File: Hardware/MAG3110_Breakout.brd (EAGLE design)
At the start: 15.2 x 15.2 mm, 18 parts, among them U1 MAG3110

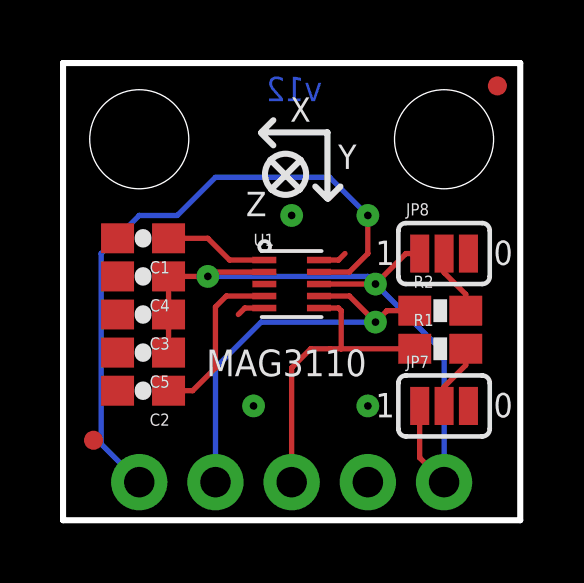
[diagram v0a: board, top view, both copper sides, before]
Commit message: Fixed pullup jumper and C3 position
Removed both three pad jumpers. Replaced with one jumper to pullup I2C
lines. Moved C3 closer to pin 8. Corrected 4 way VCC net in schematic.
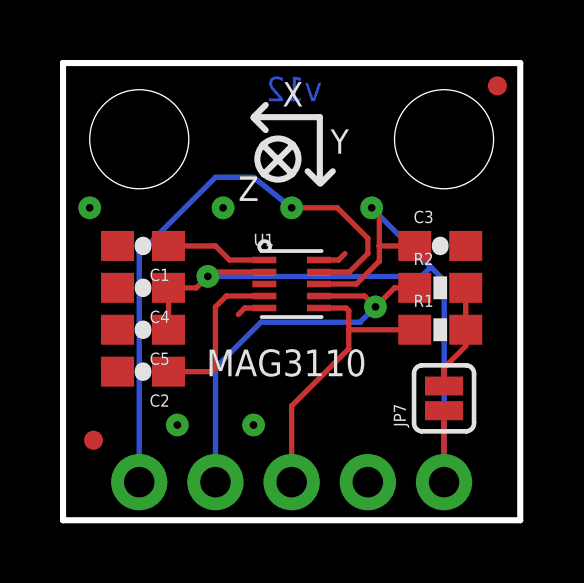
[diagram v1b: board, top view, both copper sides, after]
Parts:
- removed JP8: JUMPER-31-2, SparkFun-Passives:SJ_3_PASTE1&2
- JP7: value JUMPER-31-2 -> (none); device SparkFun-Passives:SJ_3_PASTE1&2 -> SparkFun-Passives:SJ_2S
- moved C3 10.2 mm to (12.6, 9.14), turned to 0 degrees
- moved C5 0.76 mm to (2.67, 6.35)
- moved R2 0.76 mm to (12.6, 7.75)
- moved C2 0.64 mm to (2.67, 4.95)
- moved JP4 0.63 mm to (8.43, 10.7)
- moved R1 0.63 mm to (12.6, 6.35)
- moved C4 0.38 mm to (2.67, 7.75)
- moved JP7 0.25 mm to (12.7, 4.06), turned to 90 degrees
- moved C1 0.25 mm to (2.67, 9.14)
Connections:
- removed net N$4: JP7.2, R1.2
- net GND: no longer JP7.3, JP8.3
- net N$3: now also JP7.2, R1.2; no longer JP8.2
- net VCC: no longer JP8.1
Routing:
- net VCC: track 25.7 -> 30.3 mm
- net INT: track 21.8 -> 19.5 mm
- net N$4: track 2.20 -> 0.00 mm
- net N$3: track 2.20 -> 3.57 mm
- net GND: vias 3 -> 4
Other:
- board text removed: "0"
- board text removed: "1"

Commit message: Updated main IC to 1:1
Updated footprint on main IC to 1:1 for better reflow and AOI.
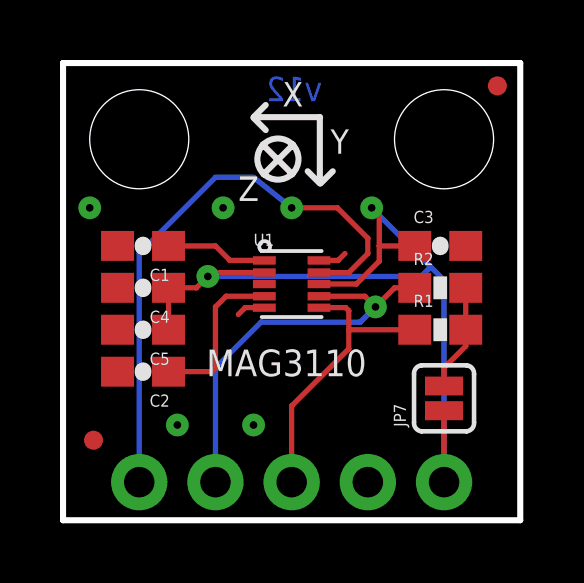
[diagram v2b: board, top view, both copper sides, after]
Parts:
- U1: value MAG3110 -> MAG31101:1; device SparkFun:DFN-10 -> SparkFun-Sensors:DFN-10-W
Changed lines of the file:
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@@
 </autorouter>
 <elements>
-<element name="U1" library="SparkFun" package="DFN-10" value="MAG3110" x="7.62" y="7.874"/>
+<element name="U1" library="SparkFun-Sensors" package="DFN-10-W" value="MAG31101:1" x="7.62" y="7.874"/>
 <element name="C1" library="SparkFun" package="0603-CAP" value="0.1uF" x="2.667" y="9.144" rot="R180"/>
 <element name="C2" library="SparkFun" package="0603-CAP" value="0.1uF" x="2.667" y="4.953" rot="R180"/>
@@
 <contactref element="U1" pad="4"/>
 <contactref element="C2" pad="1"/>
-<wire x1="6.71" y1="7.474" x2="5.442" y2="7.474" width="0.1778" layer="1"/>
-<wire x1="5.442" y1="7.474" x2="5.08" y2="7.112" width="0.1778" layer="1"/>
 <wire x1="3.517" y1="4.953" x2="4.953" y2="4.953" width="0.1778" layer="1"/>
 <wire x1="4.953" y1="4.953" x2="5.08" y2="5.08" width="0.1778" layer="1"/>
 <wire x1="5.08" y1="5.08" x2="5.08" y2="7.112" width="0.1778" layer="1"/>
+<wire x1="6.71" y1="7.46765" x2="5.43565" y2="7.46765" width="0.1778" layer="1"/>
+<wire x1="5.43565" y1="7.46765" x2="5.08" y2="7.112" width="0.1778" layer="1"/>
 </signal>
 <signal name="N$2">
 <contactref element="U1" pad="1"/>
 <contactref element="C1" pad="1"/>
-<wire x1="6.71" y1="8.674" x2="5.55" y2="8.674" width="0.1778" layer="1"/>
 <wire x1="3.517" y1="9.144" x2="5.08" y2="9.144" width="0.1778" layer="1"/>
-<wire x1="5.08" y1="9.144" x2="5.55" y2="8.674" width="0.1778" layer="1"/>
+<wire x1="6.71" y1="8.6613" x2="5.5627" y2="8.6613" width="0.1778" layer="1"/>
+<wire x1="5.5627" y1="8.6613" x2="5.08" y2="9.144" width="0.1778" layer="1"/>
 </signal>
 <signal name="GND">
@@
 <vertex x="15.24" y="15.24"/>
 </polygon>
-<wire x1="8.53" y1="8.674" x2="9.182" y2="8.674" width="0.1778" layer="1"/>
-<wire x1="9.182" y1="8.674" x2="9.398" y2="8.89" width="0.1778" layer="1"/>
-<wire x1="6.71" y1="7.074" x2="6.058" y2="7.074" width="0.1778" layer="1"/>
-<wire x1="6.058" y1="7.074" x2="5.842" y2="6.858" width="0.1778" layer="1"/>
 <via x="3.81" y="3.175" extent="1-16" drill="0.254"/>
 <via x="5.334" y="10.414" extent="1-16" drill="0.254"/>
@@
 <via x="6.35" y="3.175" extent="1-16" drill="0.254"/>
 <via x="0.889" y="10.414" extent="1-16" drill="0.254"/>
+<wire x1="6.71" y1="7.0867" x2="6.0707" y2="7.0867" width="0.1778" layer="1"/>
+<wire x1="6.0707" y1="7.0867" x2="5.842" y2="6.858" width="0.1778" layer="1"/>
+<wire x1="8.53" y1="8.6613" x2="9.1693" y2="8.6613" width="0.1778" layer="1"/>
+<wire x1="9.1693" y1="8.6613" x2="9.398" y2="8.89" width="0.1778" layer="1"/>
 </signal>
 <signal name="VCC">
@@
 <contactref element="U1" pad="8"/>
 <contactref element="JP1" pad="5"/>
-<wire x1="8.53" y1="7.874" x2="9.779" y2="7.874" width="0.1778" layer="1"/>
-<wire x1="6.71" y1="8.274" x2="4.972" y2="8.274" width="0.1778" layer="1"/>
 <via x="4.826" y="8.128" extent="1-16" drill="0.254"/>
 <contactref element="C5" pad="1"/>
@@
 <via x="10.287" y="10.414" extent="1-16" drill="0.254"/>
 <wire x1="10.541" y1="9.144" x2="10.541" y2="8.636" width="0.1778" layer="1"/>
-<wire x1="10.541" y1="8.636" x2="9.779" y2="7.874" width="0.1778" layer="1"/>
 <wire x1="11.723" y1="9.144" x2="10.541" y2="9.144" width="0.1778" layer="1"/>
-<wire x1="4.972" y1="8.274" x2="4.826" y2="8.128" width="0.1778" layer="1"/>
 <wire x1="12.7" y1="8.001" x2="12.7" y2="1.27" width="0.1778" layer="16"/>
 <wire x1="10.541" y1="9.144" x2="10.541" y2="10.16" width="0.1778" layer="1"/>
@@
 <wire x1="4.826" y1="8.128" x2="11.938" y2="8.128" width="0.1778" layer="16"/>
 <wire x1="11.938" y1="8.128" x2="12.2555" y2="8.4455" width="0.1778" layer="16"/>
+<wire x1="6.71" y1="8.25495" x2="4.95295" y2="8.25495" width="0.1778" layer="1"/>
+<wire x1="4.95295" y1="8.25495" x2="4.826" y2="8.128" width="0.1778" layer="1"/>
+<wire x1="8.53" y1="7.874" x2="9.779" y2="7.874" width="0.1778" layer="1"/>
+<wire x1="9.779" y1="7.874" x2="10.541" y2="8.636" width="0.1778" layer="1"/>
 </signal>
 <signal name="SDA">
@@
 <contactref element="R1" pad="1"/>
 <contactref element="JP1" pad="3"/>
-<wire x1="8.53" y1="7.074" x2="9.436" y2="7.074" width="0.1778" layer="1"/>
-<wire x1="9.436" y1="7.074" x2="9.525" y2="6.985" width="0.1778" layer="1"/>
 <wire x1="9.525" y1="6.985" x2="9.525" y2="6.35" width="0.1778" layer="1"/>
 <wire x1="11.723" y1="6.35" x2="9.525" y2="6.35" width="0.1778" layer="1"/>
@@
 <wire x1="9.525" y1="5.715" x2="7.62" y2="3.81" width="0.1778" layer="1"/>
 <wire x1="7.62" y1="3.81" x2="7.62" y2="1.27" width="0.1778" layer="1"/>
+<wire x1="8.53" y1="7.0867" x2="9.4233" y2="7.0867" width="0.1778" layer="1"/>
+<wire x1="9.4233" y1="7.0867" x2="9.525" y2="6.985" width="0.1778" layer="1"/>
 </signal>
 <signal name="SCL">
@@
 <contactref element="JP1" pad="2"/>
 <contactref element="U1" pad="7"/>
-<wire x1="8.53" y1="7.474" x2="10.052" y2="7.474" width="0.1778" layer="1"/>
 <via x="10.414" y="7.112" extent="1-16" drill="0.254"/>
 <wire x1="5.08" y1="5.08" x2="5.08" y2="1.27" width="0.1778" layer="16"/>
@@
 <wire x1="6.604" y1="6.604" x2="9.906" y2="6.604" width="0.1778" layer="16"/>
 <wire x1="9.906" y1="6.604" x2="10.414" y2="7.112" width="0.1778" layer="16"/>
-<wire x1="10.052" y1="7.474" x2="10.414" y2="7.112" width="0.1778" layer="1"/>
 <wire x1="11.723" y1="7.747" x2="11.049" y2="7.747" width="0.1778" layer="1"/>
 <wire x1="11.049" y1="7.747" x2="10.414" y2="7.112" width="0.1778" layer="1"/>
+<wire x1="8.53" y1="7.46765" x2="10.05835" y2="7.46765" width="0.1778" layer="1"/>
+<wire x1="10.05835" y1="7.46765" x2="10.414" y2="7.112" width="0.1778" layer="1"/>
 </signal>
 <signal name="INT">
 <contactref element="U1" pad="9"/>
 <contactref element="JP1" pad="1"/>
-<wire x1="8.53" y1="8.274" x2="9.544" y2="8.274" width="0.1778" layer="1"/>
 <via x="7.62" y="10.414" extent="1-16" drill="0.254"/>
 <wire x1="2.54" y1="1.27" x2="2.54" y2="8.89" width="0.1778" layer="16"/>
 <wire x1="2.54" y1="8.89" x2="5.08" y2="11.43" width="0.1778" layer="16"/>
-<wire x1="9.544" y1="8.274" x2="10.16" y2="8.89" width="0.1778" layer="1"/>
 <wire x1="10.16" y1="8.89" x2="10.16" y2="9.398" width="0.1778" layer="1"/>
 <wire x1="7.62" y1="10.414" x2="6.35" y2="11.43" width="0.1778" layer="16"/>
@@
 <wire x1="7.62" y1="10.414" x2="9.144" y2="10.414" width="0.1778" layer="1"/>
 <wire x1="9.144" y1="10.414" x2="10.16" y2="9.398" width="0.1778" layer="1"/>
+<wire x1="8.53" y1="8.25495" x2="9.52495" y2="8.25495" width="0.1778" layer="1"/>
+<wire x1="9.52495" y1="8.25495" x2="10.16" y2="8.89" width="0.1778" layer="1"/>
 </signal>
 <signal name="N$3">

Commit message: Modified I2C pullup solder jumper
Changed solder jumper for I2C pullup so that I2C lines will be
completely floating if jumper is open. Moved capacitor bank to the left
.005 grid spaces and moved resistors and cap on right side over .005 to
the right, all for better trace routing. Changed int trace to be more
direct to header.
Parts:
- removed JP7: (no value), SparkFun-Passives:SJ_2S
- added SJ1: (no value), SparkFun-Passives:SJ_3_PASTE1&2&3
- moved C1 0.13 mm to (2.54, 9.14)
- moved C2 0.13 mm to (2.54, 4.95)
- moved C4 0.13 mm to (2.54, 7.75)
- moved C5 0.13 mm to (2.54, 6.35)
- moved C3 0.13 mm to (12.7, 9.14)
- moved R1 0.13 mm to (12.7, 6.35)
- moved R2 0.13 mm to (12.7, 7.75)
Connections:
- new net N$4: R1.2, SJ1.3
- net N$3: now also SJ1.1; no longer JP7.2, R1.2
- net VCC: now also SJ1.2; no longer JP7.1
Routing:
- net N$4: track 0.00 -> 3.72 mm
- net N$3: track 3.57 -> 5.28 mm
- net INT: track 19.5 -> 17.9 mm
- net VCC: track 30.3 -> 30.9 mm
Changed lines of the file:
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@@
 <?xml version="1.0" encoding="utf-8"?>
 <!DOCTYPE eagle SYSTEM "eagle.dtd">
-<eagle version="6.4">
+<eagle version="6.5.0">
 <drawing>
 <settings>
@@
 <elements>
 <element name="U1" library="SparkFun-Sensors" package="DFN-10-W" value="MAG31101:1" x="7.62" y="7.874"/>
-<element name="C1" library="SparkFun" package="0603-CAP" value="0.1uF" x="2.667" y="9.144" rot="R180"/>
-<element name="C2" library="SparkFun" package="0603-CAP" value="0.1uF" x="2.667" y="4.953" rot="R180"/>
-<element name="C3" library="SparkFun" package="0603-CAP" value="0.1uF" x="12.573" y="9.144"/>
-<element name="C4" library="SparkFun" package="0603-CAP" value="1uF" x="2.667" y="7.747" rot="R180"/>
-<element name="C5" library="SparkFun" package="0603-CAP" value="0.1uF" x="2.667" y="6.35" rot="R180"/>
-<element name="R1" library="SparkFun" package="0603-RES" value="4.7k" x="12.573" y="6.35"/>
-<element name="R2" library="SparkFun" package="0603-RES" value="4.7k" x="12.573" y="7.747"/>
+<element name="C1" library="SparkFun" package="0603-CAP" value="0.1uF" x="2.54" y="9.144" rot="R180"/>
+<element name="C2" library="SparkFun" package="0603-CAP" value="0.1uF" x="2.54" y="4.953" rot="R180"/>
+<element name="C3" library="SparkFun" package="0603-CAP" value="0.1uF" x="12.7" y="9.144"/>
+<element name="C4" library="SparkFun" package="0603-CAP" value="1uF" x="2.54" y="7.747" rot="R180"/>
+<element name="C5" library="SparkFun" package="0603-CAP" value="0.1uF" x="2.54" y="6.35" rot="R180"/>
+<element name="R1" library="SparkFun" package="0603-RES" value="4.7k" x="12.7" y="6.35"/>
+<element name="R2" library="SparkFun" package="0603-RES" value="4.7k" x="12.7" y="7.747"/>
 <element name="JP1" library="SparkFun" package="1X05" value="breakout" x="2.54" y="1.27" rot="MR180"/>
 <element name="JP2" library="SparkFun" package="STAND-OFF" value="STAND-OFF" x="2.54" y="12.7"/>
@@
 <element name="FRAME2" library="SparkFun-Aesthetics" package="CREATIVE_COMMONS" value="FRAME-LETTER" x="-12.7" y="-8.89"/>
 <element name="LOGO1" library="SparkFun-Aesthetics" package="OSHW-LOGO-S" value="OSHW-LOGOS" x="7.62" y="6.604" rot="MR0"/>
-<element name="JP7" library="SparkFun-Passives" package="SJ_2S" value="" x="12.7" y="4.064" rot="R90"/>
+<element name="SJ1" library="SparkFun-Passives" package="SJ_3_PASTE1&amp;2&amp;3" value="" x="12.7" y="4.064" rot="R180"/>
 </elements>
 <signals>
@@
 <contactref element="U1" pad="4"/>
 <contactref element="C2" pad="1"/>
-<wire x1="3.517" y1="4.953" x2="4.953" y2="4.953" width="0.1778" layer="1"/>
-<wire x1="4.953" y1="4.953" x2="5.08" y2="5.08" width="0.1778" layer="1"/>
-<wire x1="5.08" y1="5.08" x2="5.08" y2="7.112" width="0.1778" layer="1"/>
+<wire x1="3.39" y1="4.953" x2="4.699" y2="4.953" width="0.1778" layer="1"/>
+<wire x1="5.08" y1="5.334" x2="5.08" y2="7.112" width="0.1778" layer="1"/>
 <wire x1="6.71" y1="7.46765" x2="5.43565" y2="7.46765" width="0.1778" layer="1"/>
 <wire x1="5.43565" y1="7.46765" x2="5.08" y2="7.112" width="0.1778" layer="1"/>
+<wire x1="5.08" y1="5.334" x2="4.699" y2="4.953" width="0.1778" layer="1"/>
 </signal>
 <signal name="N$2">
 <contactref element="U1" pad="1"/>
 <contactref element="C1" pad="1"/>
-<wire x1="3.517" y1="9.144" x2="5.08" y2="9.144" width="0.1778" layer="1"/>
+<wire x1="3.39" y1="9.144" x2="5.08" y2="9.144" width="0.1778" layer="1"/>
 <wire x1="6.71" y1="8.6613" x2="5.5627" y2="8.6613" width="0.1778" layer="1"/>
 <wire x1="5.5627" y1="8.6613" x2="5.08" y2="9.144" width="0.1778" layer="1"/>
@@
 </polygon>
 <via x="3.81" y="3.175" extent="1-16" drill="0.254"/>
-<via x="5.334" y="10.414" extent="1-16" drill="0.254"/>
+<via x="4.953" y="10.414" extent="1-16" drill="0.254"/>
 <contactref element="C4" pad="2"/>
 <contactref element="C5" pad="2"/>
@@
 <contactref element="C5" pad="1"/>
 <contactref element="C4" pad="1"/>
-<contactref element="JP7" pad="1"/>
-<wire x1="3.517" y1="6.35" x2="3.517" y2="7.747" width="0.1778" layer="1"/>
-<wire x1="3.517" y1="7.747" x2="4.445" y2="7.747" width="0.1778" layer="1"/>
+<wire x1="3.39" y1="6.35" x2="3.39" y2="7.747" width="0.1778" layer="1"/>
+<wire x1="3.39" y1="7.747" x2="4.445" y2="7.747" width="0.1778" layer="1"/>
 <wire x1="4.445" y1="7.747" x2="4.826" y2="8.128" width="0.1778" layer="1"/>
-<wire x1="12.7" y1="3.6521" x2="12.7" y2="1.27" width="0.1778" layer="1"/>
 <via x="10.287" y="10.414" extent="1-16" drill="0.254"/>
 <wire x1="10.541" y1="9.144" x2="10.541" y2="8.636" width="0.1778" layer="1"/>
-<wire x1="11.723" y1="9.144" x2="10.541" y2="9.144" width="0.1778" layer="1"/>
+<wire x1="11.85" y1="9.144" x2="10.541" y2="9.144" width="0.1778" layer="1"/>
 <wire x1="12.7" y1="8.001" x2="12.7" y2="1.27" width="0.1778" layer="16"/>
 <wire x1="10.541" y1="9.144" x2="10.541" y2="10.16" width="0.1778" layer="1"/>
@@
 <wire x1="8.53" y1="7.874" x2="9.779" y2="7.874" width="0.1778" layer="1"/>
 <wire x1="9.779" y1="7.874" x2="10.541" y2="8.636" width="0.1778" layer="1"/>
+<contactref element="SJ1" pad="2"/>
+<wire x1="12.7" y1="4.064" x2="12.7" y2="1.27" width="0.1778" layer="1"/>
 </signal>
 <signal name="SDA">
-<contactref element="U1" pad="6"/>
-<contactref element="R1" pad="1"/>
 <contactref element="JP1" pad="3"/>
 <wire x1="9.525" y1="6.985" x2="9.525" y2="6.35" width="0.1778" layer="1"/>
-<wire x1="11.723" y1="6.35" x2="9.525" y2="6.35" width="0.1778" layer="1"/>
 <wire x1="9.525" y1="6.35" x2="9.525" y2="5.715" width="0.1778" layer="1"/>
 <wire x1="9.525" y1="5.715" x2="7.62" y2="3.81" width="0.1778" layer="1"/>
 <wire x1="7.62" y1="3.81" x2="7.62" y2="1.27" width="0.1778" layer="1"/>
+<wire x1="9.4233" y1="7.0867" x2="9.525" y2="6.985" width="0.1778" layer="1"/>
+<contactref element="R1" pad="1"/>
+<contactref element="U1" pad="6"/>
 <wire x1="8.53" y1="7.0867" x2="9.4233" y2="7.0867" width="0.1778" layer="1"/>
-<wire x1="9.4233" y1="7.0867" x2="9.525" y2="6.985" width="0.1778" layer="1"/>
+<wire x1="11.85" y1="6.35" x2="9.525" y2="6.35" width="0.1778" layer="1"/>
 </signal>
 <signal name="SCL">
@@
 <wire x1="6.604" y1="6.604" x2="9.906" y2="6.604" width="0.1778" layer="16"/>
 <wire x1="9.906" y1="6.604" x2="10.414" y2="7.112" width="0.1778" layer="16"/>
-<wire x1="11.723" y1="7.747" x2="11.049" y2="7.747" width="0.1778" layer="1"/>
-<wire x1="11.049" y1="7.747" x2="10.414" y2="7.112" width="0.1778" layer="1"/>
 <wire x1="8.53" y1="7.46765" x2="10.05835" y2="7.46765" width="0.1778" layer="1"/>
 <wire x1="10.05835" y1="7.46765" x2="10.414" y2="7.112" width="0.1778" layer="1"/>
+<wire x1="11.85" y1="7.747" x2="11.049" y2="7.747" width="0.1778" layer="1"/>
+<wire x1="11.049" y1="7.747" x2="10.414" y2="7.112" width="0.1778" layer="1"/>
 </signal>
 <signal name="INT">
@@
 <contactref element="JP1" pad="1"/>
 <via x="7.62" y="10.414" extent="1-16" drill="0.254"/>
-<wire x1="2.54" y1="1.27" x2="2.54" y2="8.89" width="0.1778" layer="16"/>
-<wire x1="2.54" y1="8.89" x2="5.08" y2="11.43" width="0.1778" layer="16"/>
+<wire x1="2.54" y1="1.27" x2="2.54" y2="7.62" width="0.1778" layer="16"/>
 <wire x1="10.16" y1="8.89" x2="10.16" y2="9.398" width="0.1778" layer="1"/>
-<wire x1="7.62" y1="10.414" x2="6.35" y2="11.43" width="0.1778" layer="16"/>
-<wire x1="6.35" y1="11.43" x2="5.08" y2="11.43" width="0.1778" layer="16"/>
 <wire x1="7.62" y1="10.414" x2="9.144" y2="10.414" width="0.1778" layer="1"/>
 <wire x1="9.144" y1="10.414" x2="10.16" y2="9.398" width="0.1778" layer="1"/>
 <wire x1="8.53" y1="8.25495" x2="9.52495" y2="8.25495" width="0.1778" layer="1"/>
 <wire x1="9.52495" y1="8.25495" x2="10.16" y2="8.89" width="0.1778" layer="1"/>
+<wire x1="7.62" y1="10.414" x2="6.604" y2="10.414" width="0.1778" layer="16"/>
+<wire x1="6.604" y1="10.414" x2="5.08" y2="8.89" width="0.1778" layer="16"/>
+<wire x1="5.08" y1="8.89" x2="3.81" y2="8.89" width="0.1778" layer="16"/>
+<wire x1="3.81" y1="8.89" x2="2.54" y2="7.62" width="0.1778" layer="16"/>
 </signal>
 <signal name="N$3">
 <contactref element="R2" pad="2"/>
+<contactref element="SJ1" pad="1"/>
+<wire x1="13.55" y1="7.747" x2="14.224" y2="7.747" width="0.1778" layer="1"/>
+<wire x1="14.224" y1="7.747" x2="14.478" y2="7.493" width="0.1778" layer="1"/>
+<wire x1="14.478" y1="7.493" x2="14.478" y2="4.318" width="0.1778" layer="1"/>
+<wire x1="14.478" y1="4.318" x2="14.224" y2="4.064" width="0.1778" layer="1"/>
+<wire x1="14.224" y1="4.064" x2="13.5128" y2="4.064" width="0.1778" layer="1"/>
+</signal>
+<signal name="N$4">
 <contactref element="R1" pad="2"/>
-<contactref element="JP7" pad="2"/>
-<wire x1="13.423" y1="7.747" x2="13.423" y2="6.35" width="0.1778" layer="1"/>
-<wire x1="12.7" y1="4.4759" x2="12.7" y2="5.08" width="0.1778" layer="1"/>
-<wire x1="13.423" y1="6.35" x2="13.423" y2="5.803" width="0.1778" layer="1"/>
-<wire x1="13.423" y1="5.803" x2="12.7" y2="5.08" width="0.1778" layer="1"/>
+<contactref element="SJ1" pad="3"/>
+<wire x1="13.55" y1="6.35" x2="13.55" y2="5.295" width="0.1778" layer="1"/>
+<wire x1="13.55" y1="5.295" x2="13.335" y2="5.08" width="0.1778" layer="1"/>
+<wire x1="11.8872" y1="4.064" x2="11.8872" y2="4.9022" width="0.1778" layer="1"/>
+<wire x1="11.8872" y1="4.9022" x2="12.065" y2="5.08" width="0.1778" layer="1"/>
+<wire x1="12.065" y1="5.08" x2="13.335" y2="5.08" width="0.1778" layer="1"/>
 </signal>
 </signals>

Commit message: Reordered Pinout
1.) Reordered pinout to adhere to new I2C layout standard
2.) Added "fake trace" to NC leg of IC for more uniform heat
distribution.
3.) Minor trace efficiency edits
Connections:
- net GND: now also JP1.1; no longer JP1.4
- net INT: now also JP1.5; no longer JP1.1
- net SCL: now also JP1.4; no longer JP1.2
- net VCC: now also JP1.2; no longer JP1.5
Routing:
- net VCC: track 30.9 -> 36.0 mm
- net SCL: track 13.7 -> 9.76 mm
- net N$4: track 3.72 -> 5.20 mm
- net N$5: track 0.00 -> 1.14 mm
- net SDA: track 9.87 -> 10.2 mm, vias 0 -> 1
- net GND: vias 4 -> 3
